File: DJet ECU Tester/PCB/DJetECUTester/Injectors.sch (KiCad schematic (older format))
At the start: 48 parts, among them Q10 MMBT2222ALT1G, Q11 MMBT2222ALT1G, Q12 MMBT2222ALT1G, Q9 MMBT2222ALT1G

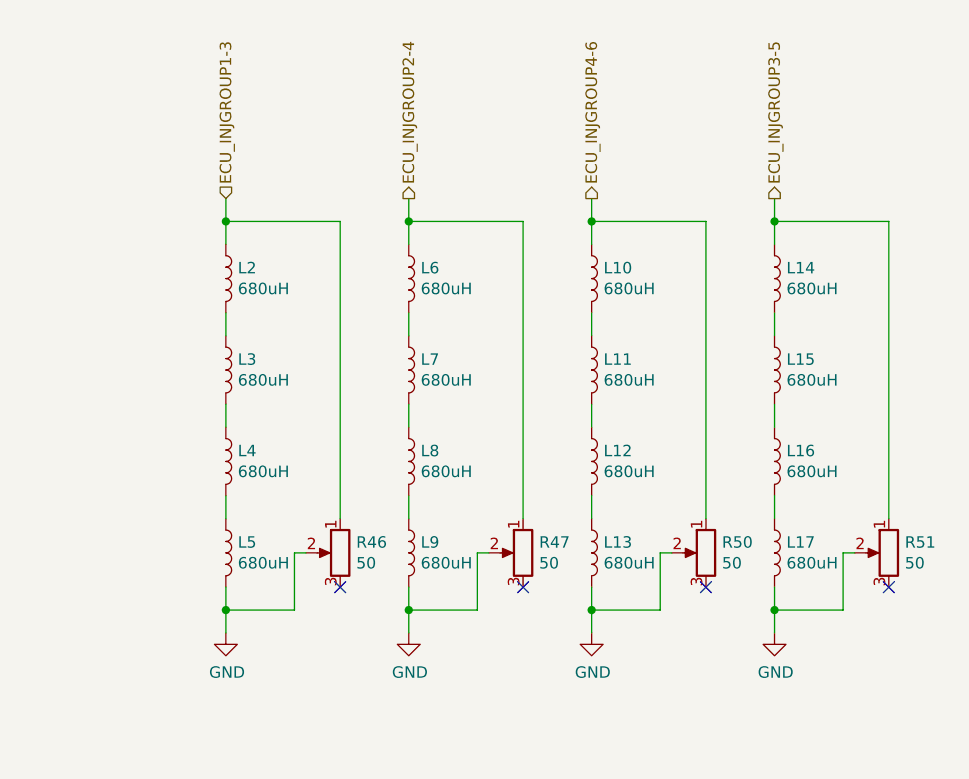
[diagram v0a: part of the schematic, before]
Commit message: Added test points from trimpots. Added ground stitching vias around inductors.
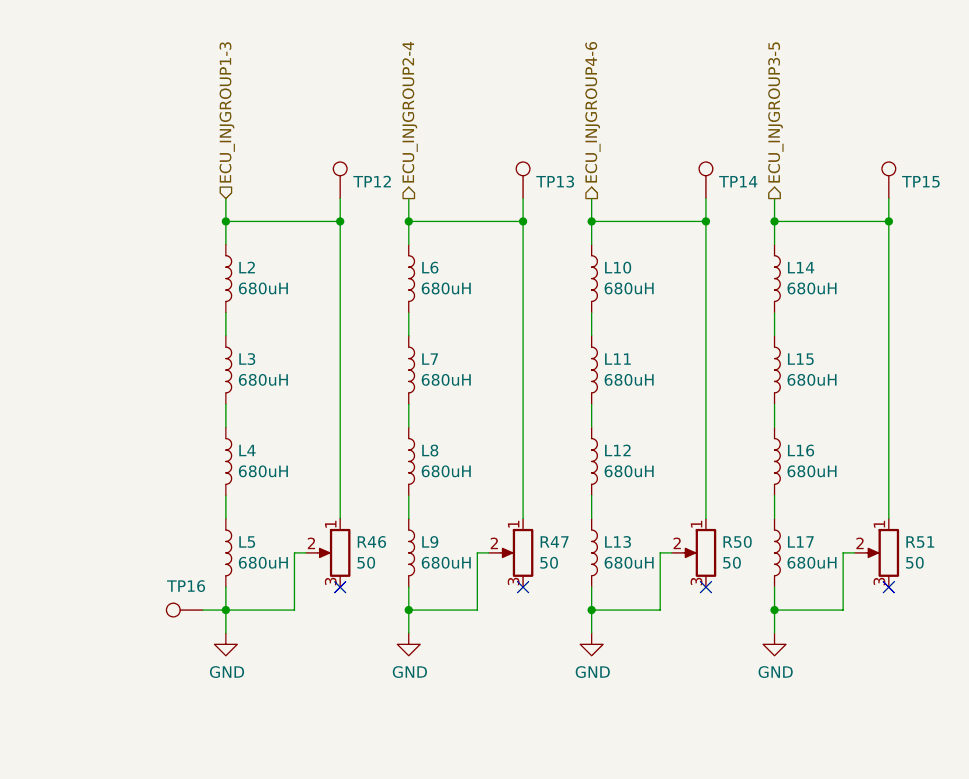
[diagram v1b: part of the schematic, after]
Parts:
- added TP12, TP13, TP14, TP15, TP16: TestPoint, TestPoint:TestPoint_Pad_D2.0mm, symbol Connector:TestPoint
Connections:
- net ECU_INJGROUP1-3: now also TP12.1
- net ECU_INJGROUP2-4: now also TP13.1
- net ECU_INJGROUP3-5: now also TP15.1
- net ECU_INJGROUP4-6: now also TP14.1
- net GND: now also TP16.1
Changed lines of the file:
@@
 Wire Wire Line
 	7050 4300 7050 3000
-Wire Wire Line
-	7050 3000 6550 3000
 Connection ~ 6550 3000
 Wire Wire Line
@@
 Wire Wire Line
 	9250 4700 8950 4700
+$Comp
+L Connector:TestPoint TP12
+U 1 1 63338C46
+P 7050 2900
+F 0 "TP12" H 7108 2972 50  0000 L CNN
+F 1 "TestPoint" H 7108 2927 50  0001 L CNN
+F 2 "TestPoint:TestPoint_Pad_D2.0mm" H 7250 2900 50  0001 C CNN
+F 3 "~" H 7250 2900 50  0001 C CNN
+	1    7050 2900
+	1    0    0    -1
+$EndComp
+$Comp
+L Connector:TestPoint TP13
+U 1 1 6333D927
+P 7850 2900
+F 0 "TP13" H 7908 2972 50  0000 L CNN
+F 1 "TestPoint" H 7908 2927 50  0001 L CNN
+F 2 "TestPoint:TestPoint_Pad_D2.0mm" H 8050 2900 50  0001 C CNN
+F 3 "~" H 8050 2900 50  0001 C CNN
+	1    7850 2900
+	1    0    0    -1
+$EndComp
+$Comp
+L Connector:TestPoint TP14
+U 1 1 6333E0A1
+P 8650 2900
+F 0 "TP14" H 8708 2972 50  0000 L CNN
+F 1 "TestPoint" H 8708 2927 50  0001 L CNN
+F 2 "TestPoint:TestPoint_Pad_D2.0mm" H 8850 2900 50  0001 C CNN
+F 3 "~" H 8850 2900 50  0001 C CNN
+	1    8650 2900
+	1    0    0    -1
+$EndComp
+$Comp
+L Connector:TestPoint TP15
+U 1 1 6333E527
+P 9450 2900
+F 0 "TP15" H 9508 2972 50  0000 L CNN
+F 1 "TestPoint" H 9508 2927 50  0001 L CNN
+F 2 "TestPoint:TestPoint_Pad_D2.0mm" H 9650 2900 50  0001 C CNN
+F 3 "~" H 9650 2900 50  0001 C CNN
+	1    9450 2900
+	1    0    0    -1
+$EndComp
+Wire Wire Line
+	6550 3000 7050 3000
+Wire Wire Line
+	7050 2900 7050 3000
+Connection ~ 7050 3000
+Wire Wire Line
+	7850 2900 7850 3000
+Connection ~ 7850 3000
+Wire Wire Line
+	8650 2900 8650 3000
+Connection ~ 8650 3000
+Wire Wire Line
+	9450 2900 9450 3000
+Connection ~ 9450 3000
+$Comp
+L Connector:TestPoint TP16
+U 1 1 6335A45A
+P 6450 4700
+F 0 "TP16" V 6553 4772 50  0000 C CNN
+F 1 "TestPoint" H 6508 4727 50  0001 L CNN
+F 2 "TestPoint:TestPoint_Pad_D2.0mm" H 6650 4700 50  0001 C CNN
+F 3 "~" H 6650 4700 50  0001 C CNN
+	1    6450 4700
+	0    -1   -1   0
+$EndComp
+Wire Wire Line
+	6450 4700 6550 4700
 $EndSCHEMATC
